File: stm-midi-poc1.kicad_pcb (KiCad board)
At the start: 4 copper layers, 100 x 100 mm, 117 parts, among them CN1 MIDI Out 1, CN2 MIDI In 1, CN3 MIDI Out 2, CN4 MIDI In 2, CN5 Line out, CN6 Headphone, J1 GT-USB-7010I, J2 SWD, J3 I2C, J4 UART46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

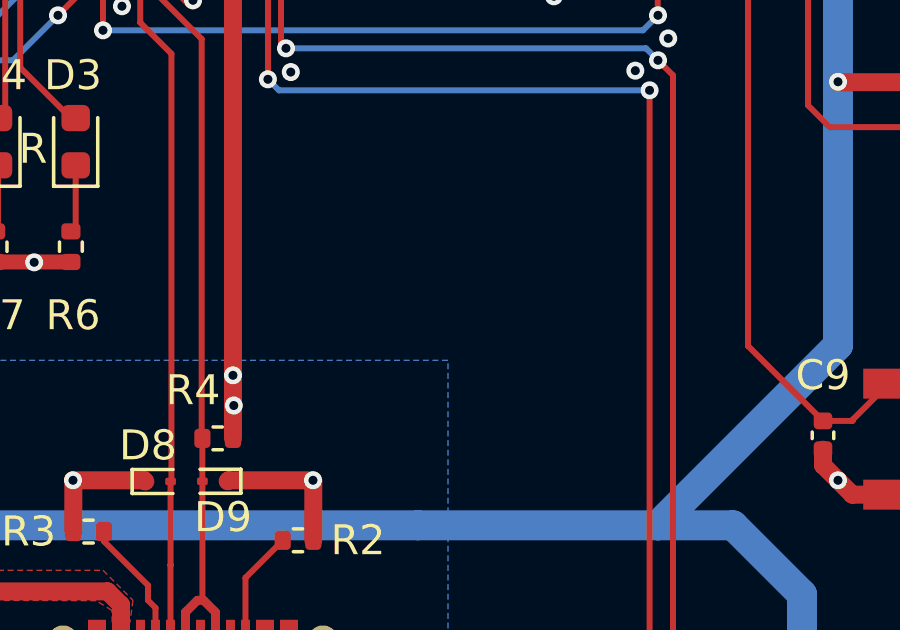
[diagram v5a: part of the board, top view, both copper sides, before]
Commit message: Added logo silk screen/footprint, exported some files (not final)
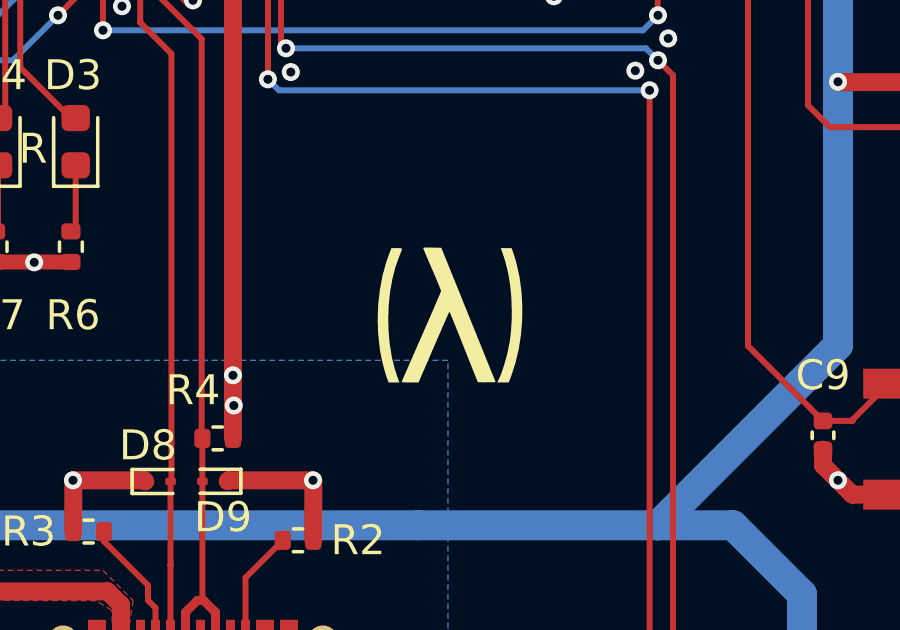
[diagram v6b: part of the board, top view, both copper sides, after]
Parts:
- added G***: LOGO, stm-midi-poc1:lispengineer-logo, F.Cu at (183.0, 119.5)
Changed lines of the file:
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@@
 	(title_block
 		(title "DPF STM MIDI PoC 1")
-		(date "2024-10-12")
+		(date "2024-10-25")
 		(rev "1")
 		(company "Douglas P. Fields, Jr.")
@@
 		(comment 3 "License: CC BY-SA 4.0")
 		(comment 4 "Copyright 2024 Douglas P. Fields, Jr.")
+		(comment 5 "EVT #1")
 	)
 	(layers
@@
 		)
 	)
+	(footprint "stm-midi-poc1:lispengineer-logo"
+		(layer "F.Cu")
+		(at 183 119.5)
+		(property "Reference" "G***"
+			(at 0 0 0)
+			(layer "F.SilkS")
+			(hide yes)
+			(effects
+				(font
+					(size 1.5 1.5)
+					(thickness 0.3)
+				)
+			)
+		)
+		(property "Value" "LOGO"
+			(at 0.75 0 0)
+			(layer "F.SilkS")
+			(hide yes)
+			(effects
+				(font
+					(size 1.5 1.5)
+					(thickness 0.3)
+				)
+			)
+		)
+		(property "Footprint" "stm-midi-poc1:lispengineer-logo"
+			(at 0 0 0)
+			(layer "F.Fab")
+			(hide yes)
+			(effects
+				(font
+					(size 1.27 1.27)
+					(thickness 0.15)
+				)
+			)
+		)
+		(property "Datasheet" ""
+			(at 0 0 0)
+			(layer "F.Fab")
+			(hide yes)
+			(effects
+				(font
+					(size 1.27 1.27)
+					(thickness 0.15)
+				)
+			)
+		)
+		(property "Description" ""
+			(at 0 0 0)
+			(layer "F.Fab")
+			(hide yes)
+			(effects
+				(font
+					(size 1.27 1.27)
+					(thickness 0.15)
+				)
+			)
+		)
+		(attr board_only exclude_from_pos_files exclude_from_bom)
+		(fp_poly
+			(pts
+				(xy -1.571648 -2.238301) (xy -1.542957 -2.226122) (xy -1.536526 -2.197187) (xy -1.550563 -2.144642)
+				(xy -1.583277 -2.061632) (xy -1.62804 -1.953164) (xy -1.756302 -1.587863) (xy -1.856867 -1.192898)
+				(xy -1.929622 -0.775644) (xy -1.974454 -0.343475) (xy -1.991252 0.096233) (xy -1.979904 0.536108)
+				(xy -1.940296 0.968774) (xy -1.872316 1.386857) (xy -1.775853 1.782982) (xy -1.689025 2.049562)
+				(xy -1.61959 2.239818) (xy -1.800029 2.239818) (xy -1.980468 2.239818) (xy -2.038699 2.082719) (xy -2.082993 1.949347)
+				(xy -2.130077 1.783842) (xy -2.176634 1.599847) (xy -2.219351 1.411005) (xy -2.254914 1.230962)
+				(xy -2.274701 1.111239) (xy -2.32805 0.618689) (xy -2.344641 0.121741) (xy -2.325112 -0.373059)
+				(xy -2.270099 -0.859169) (xy -2.18024 -1.330044) (xy -2.056171 -1.779142) (xy -1.969282 -2.02577)
+				(xy -1.887353 -2.239819) (xy -1.702983 -2.239819) (xy -1.624393 -2.240582)
+			)
+			(stroke
+				(width 0)
+				(type solid)
+			)
+			(fill solid)
+			(layer "F.SilkS")
+		)
+		(fp_poly
+			(pts
+				(xy 2.16813 -2.108702) (xy 2.19533 -2.030437) (xy 2.228841 -1.923476) (xy 2.263747 -1.803919) (xy 2.286226 -1.721929)
+				(xy 2.385623 -1.268806) (xy 2.449579 -0.796838) (xy 2.478445 -0.313322) (xy 2.472569 0.174444) (xy 2.4323 0.659162)
+				(xy 2.357987 1.133533) (xy 2.249978 1.590261) (xy 2.108623 2.022046) (xy 2.107037 2.026227) (xy 2.025898 2.239818)
+				(xy 1.832287 2.239818) (xy 1.638676 2.239818) (xy 1.69565 2.127386) (xy 1.740215 2.027274) (xy 1.791079 1.893071)
+				(xy 1.844687 1.735805) (xy 1.897483 1.566503) (xy 1.945911 1.396192) (xy 1.986417 1.235899) (xy 1.994435 1.200727)
+				(xy 2.057363 0.870498) (xy 2.099447 0.534444) (xy 2.122033 0.179178) (xy 2.126986 -0.11561) (xy 2.110779 -0.60814)
+				(xy 2.063083 -1.073212) (xy 1.984239 -1.508648) (xy 1.874585 -1.912272) (xy 1.825028 -2.056526)
+				(xy 1.758135 -2.239818) (xy 1.938044 -2.239818) (xy 2.117954 -2.239818)
+			)
+			(stroke
+				(width 0)
+				(type solid)
+			)
+			(fill solid)
+			(layer "F.SilkS")
+		)
+		(fp_poly
+			(pts
+				(xy -0.550336 -2.258286) (xy -0.528032 -2.257819) (xy -0.221245 -2.251364) (xy 0.683926 -0.011546)
+				(xy 1.589097 2.228272) (xy 1.298649 2.234764) (xy 1.187238 2.235871) (xy 1.093094 2.234198) (xy 1.02554 2.230098)
+				(xy 0.993899 2.223924) (xy 0.993079 2.223219) (xy 0.982008 2.198904) (xy 0.955686 2.13557) (xy 0.915708 2.037201)
+				(xy 0.863666 1.907777) (xy 0.801153 1.751283) (xy 0.729761 1.571699) (xy 0.651084 1.373009) (xy 0.566714 1.159194)
+				(xy 0.517842 1.035018) (xy 0.431261 0.815711) (xy 0.349507 0.610349) (xy 0.274157 0.422767) (xy 0.206783 0.256804)
+				(xy 0.148959 0.116295) (xy 0.10226 0.005079) (xy 0.068259 -0.073008) (xy 0.04853 -0.11413) (xy 0.044244 -0.119527)
+				(xy 0.032811 -0.09598) (xy 0.004807 -0.033908) (xy -0.038064 0.062799) (xy -0.094101 0.190253) (xy -0.161601 0.344566)
+				(xy -0.238861 0.521848) (xy -0.32418 0.718211) (xy -0.415855 0.929766) (xy -0.475302 1.067233) (xy -0.981364 2.238375)
+				(xy -1.264228 2.239096) (xy -1.372389 2.238366) (xy -1.461458 2.235848) (xy -1.522601 2.231931)
+				(xy -1.546989 2.227004) (xy -1.547091 2.226649) (xy -1.538024 2.203862) (xy -1.51181 2.14222) (xy -1.469934 2.045123)
+				(xy -1.413879 1.915974) (xy -1.345129 1.758175) (xy -1.265167 1.575127) (xy -1.175478 1.370231)
+				(xy -1.077545 1.14689) (xy -0.972852 0.908505) (xy -0.889 0.717828) (xy -0.779998 0.469638) (xy -0.676636 0.233396)
+				(xy -0.580402 0.012562) (xy -0.492787 -0.189404) (xy -0.41528 -0.369041) (xy -0.349369 -0.52289)
+				(xy -0.296544 -0.647491) (xy -0.258294 -0.739383) (xy -0.23611 -0.795107) (xy -0.230909 -0.811105)
+				(xy -0.239799 -0.839846) (xy -0.264984 -0.90549) (xy -0.304238 -1.002635) (xy -0.355333 -1.125879)
+				(xy -0.416042 -1.269822) (xy -0.484139 -1.429061) (xy -0.518006 -1.507516) (xy -0.589459 -1.672946)
+				(xy -0.655374 -1.826299) (xy -0.713389 -1.962019) (xy -0.761142 -2.074552) (xy -0.796271 -2.158346)
+				(xy -0.816412 -2.207845) (xy -0.81996 -2.21746) (xy -0.824132 -2.236324) (xy -0.81791 -2.249086)
+				(xy -0.794355 -2.256704) (xy -0.746533 -2.260137) (xy -0.667506 -2.260345)
+			)
+			(stroke
+				(width 0)
+				(type solid)
+			)
+			(fill solid)
+			(layer "F.SilkS")
+		)
+	)

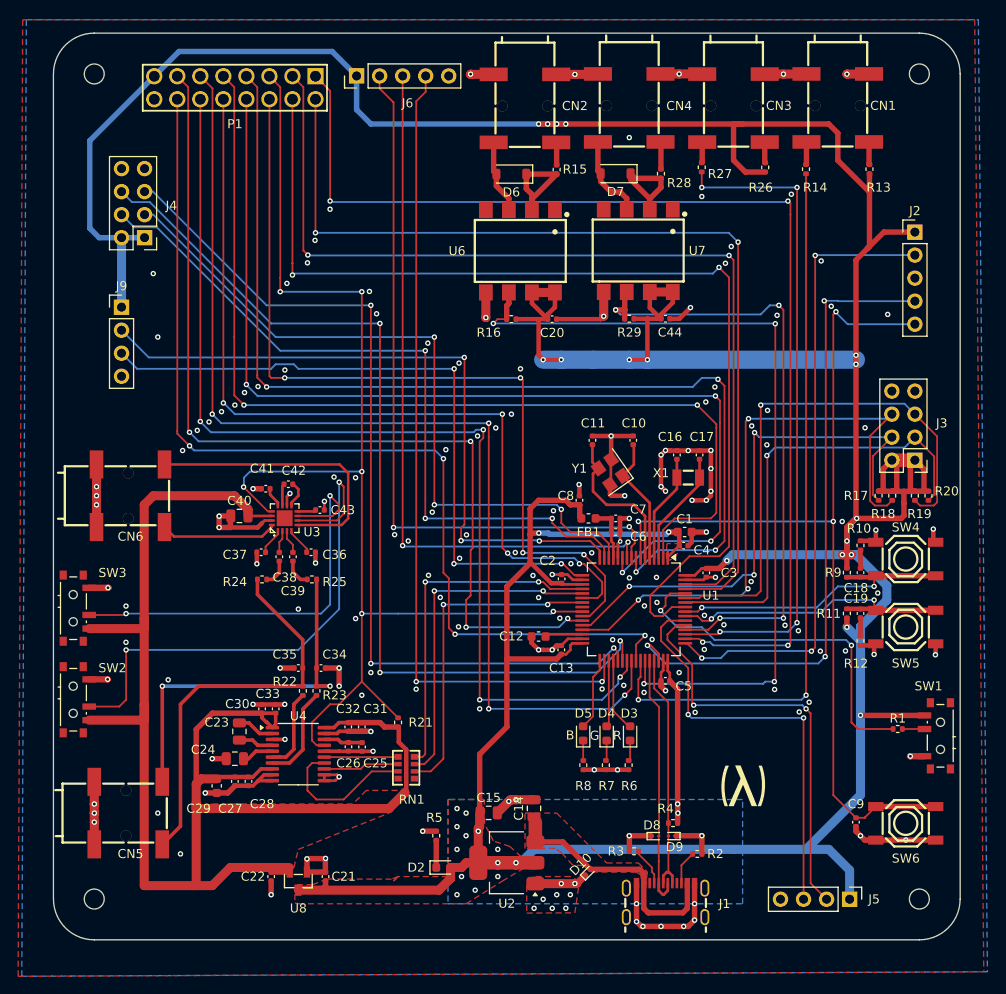
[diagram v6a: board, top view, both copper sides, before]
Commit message: 1. Update README with info on my KiCAD component library. 2. Add Fiducial markers. 3. Add LCSC IDs for all parts in BOM.
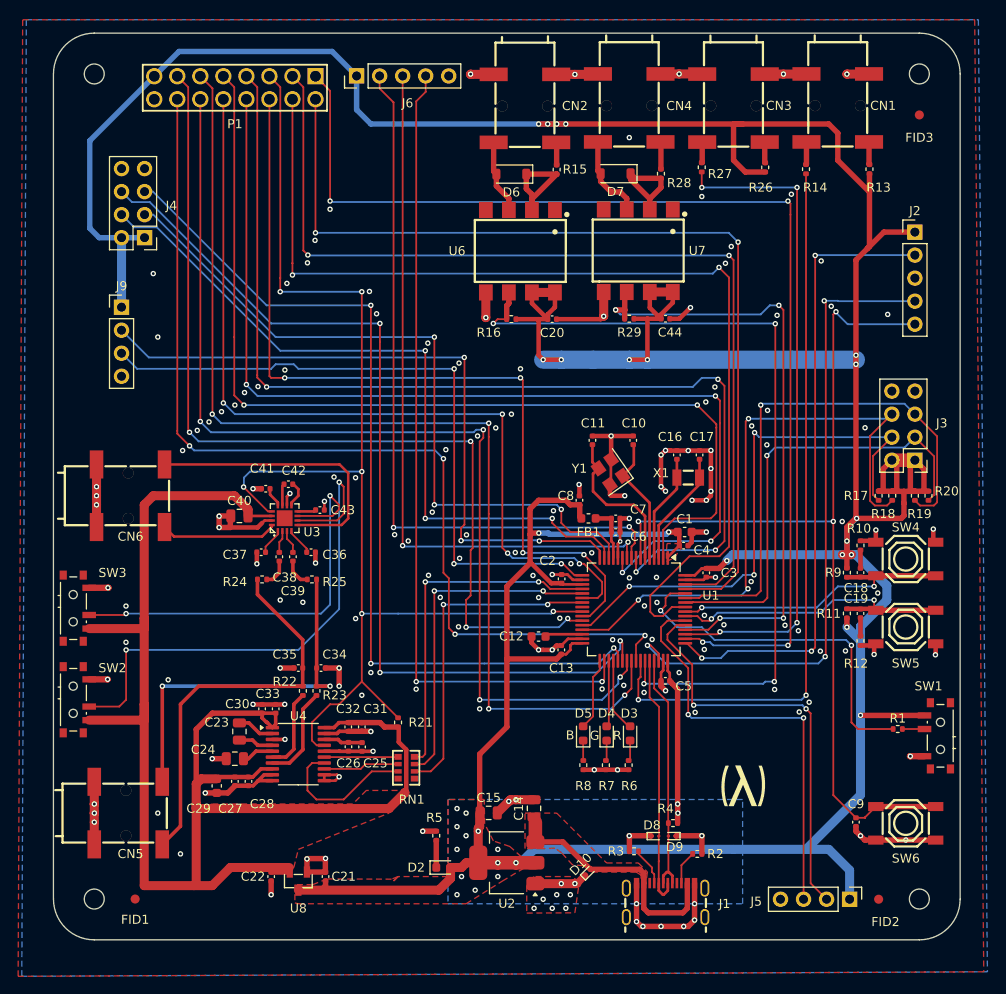
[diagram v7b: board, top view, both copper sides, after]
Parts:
- added FID1: Fiducial, Fiducial:Fiducial_1mm_Mask2mm, F.Cu at (116.0, 132.0)
- added FID2: Fiducial, Fiducial:Fiducial_1mm_Mask2mm, F.Cu at (198.0, 132.0)
- added FID3: Fiducial, Fiducial:Fiducial_1mm_Mask2mm, F.Cu at (202.5, 45.5)
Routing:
- net GND: vias 177 -> 178
